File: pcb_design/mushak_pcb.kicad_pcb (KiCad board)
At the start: 2 copper layers, 57.7 x 40 mm, 123 parts, among them J1 Conn_01x04_Male, J10 IR_1, J11 AS5600_1, J12 IR_2, J13 AS5600_2, J14 IR_3, J15 ToF, J16 IR_4, J17 ToF, J2 Conn_01x02_Female, J3 BLE_Conn, J4 AS5600_Left, J5 AS5600_Right, J6 IR_1, J7 IR_3, J8 IR_2, J9 IR_4, M1 motor, M2 motor, Q1 DMN3065LW-7, Q2 DMN3065LW-7, Q3 DMN3065LW-7, Q4 DMN3065LW-7, Q5 DMN3065LW-7, SW1 SW_Push, SW2 SW_Push, U1 BA30BC0FP-E2, U2 AS5048B-HTSP, U3 DRV8833PW, U4 VL6180XV0NR/1, U5 MPU-6500, U6 STM32F405RGTx, U7 AS5048B-HTSP, Y1 25Mhz, Y2 32.769kHz

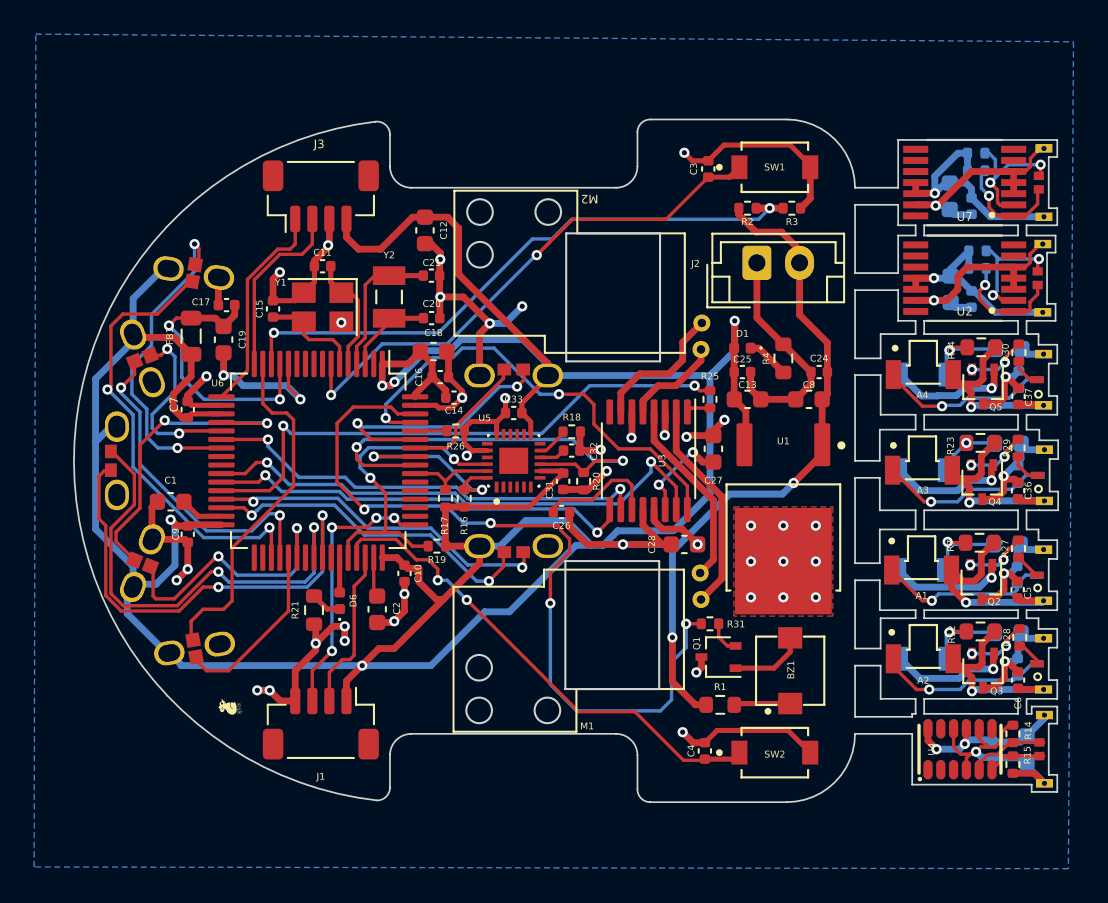
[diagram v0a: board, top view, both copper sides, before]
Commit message: Update PCB as per manufacturing requirements
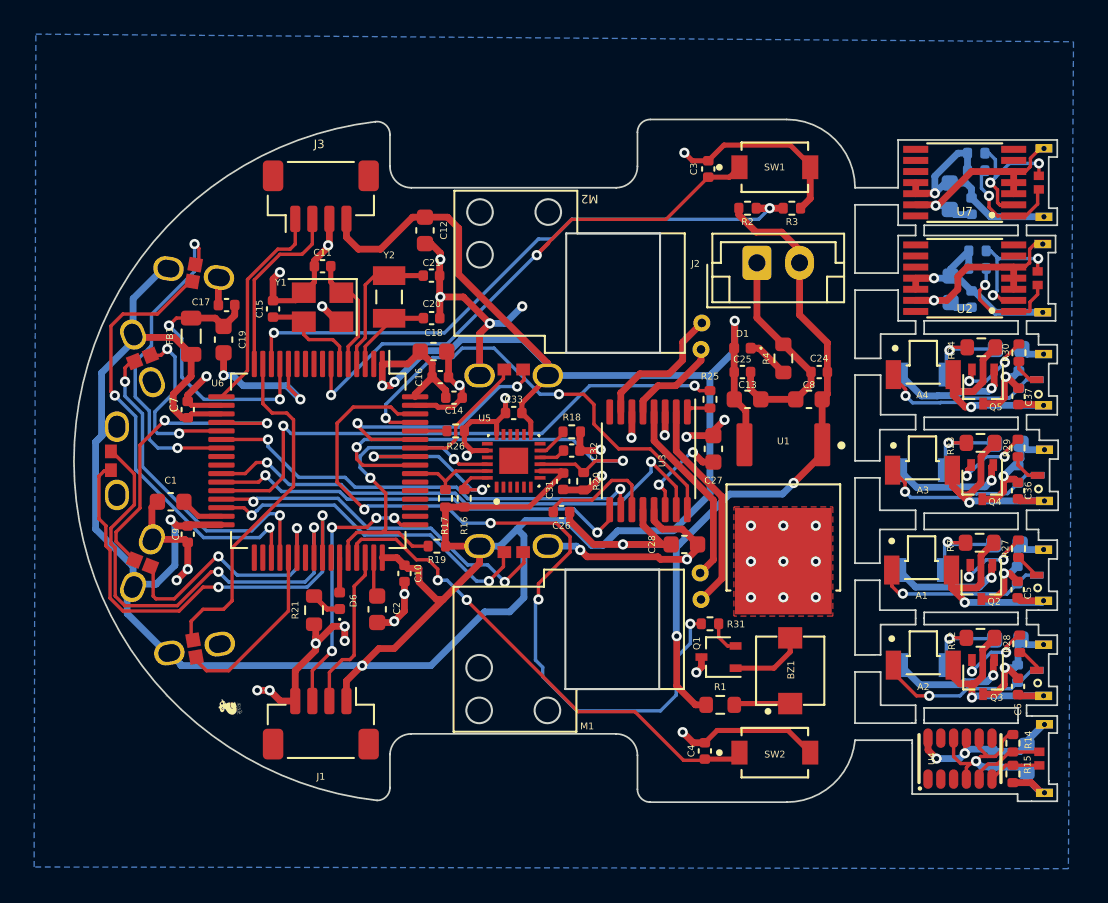
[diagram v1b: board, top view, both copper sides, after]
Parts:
- moved C29 0.55 mm to (204.1, 114.5)
- moved C30 0.55 mm to (202.1, 114.5)
- moved J17 0.55 mm to (205.3, 114.5)
- moved R14 0.55 mm to (203.2, 113.5)
- moved R15 0.55 mm to (203.2, 115.3)
- moved U4 0.55 mm to (200.2, 114.5)
- moved A2 0.37 mm to (198.0, 109.0)
- moved C35 0.37 mm to (202.9, 107.5)
- moved C6 0.37 mm to (203.6, 110.2)
- moved D3 0.37 mm to (198.0, 109.0)
- moved J7 0.37 mm to (205.3, 109.3)
- moved Q3 0.37 mm to (201.5, 109.7)
- moved R11 0.37 mm to (203.5, 109.5)
- moved R12 0.37 mm to (201.3, 107.4)
- moved R28 0.37 mm to (203.7, 107.7)
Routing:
- net POW_GND: track 121.3 -> 132.1 mm, vias 41 -> 42
- net /IR_sensor/+3V0_3: track 12.6 -> 14.4 mm
- net Net-(C38-Pad1): track 3.78 -> 5.44 mm
- net /IR_sensor/+3V0_4: track 12.5 -> 14.0 mm
- net Net-(Q4-Pad2): track 3.51 -> 4.76 mm
- net Net-(Q5-Pad2): track 3.52 -> 4.71 mm
- net Net-(Q2-Pad2): track 3.60 -> 4.69 mm
- net +3V0: track 196.7 -> 195.6 mm
- net Net-(Q3-Pad2): track 3.58 -> 4.54 mm
- net BUZZER_OP: track 46.5 -> 47.1 mm
- net SCL_2: track 20.4 -> 21.0 mm
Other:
- outline, holes or cut-outs redrawn

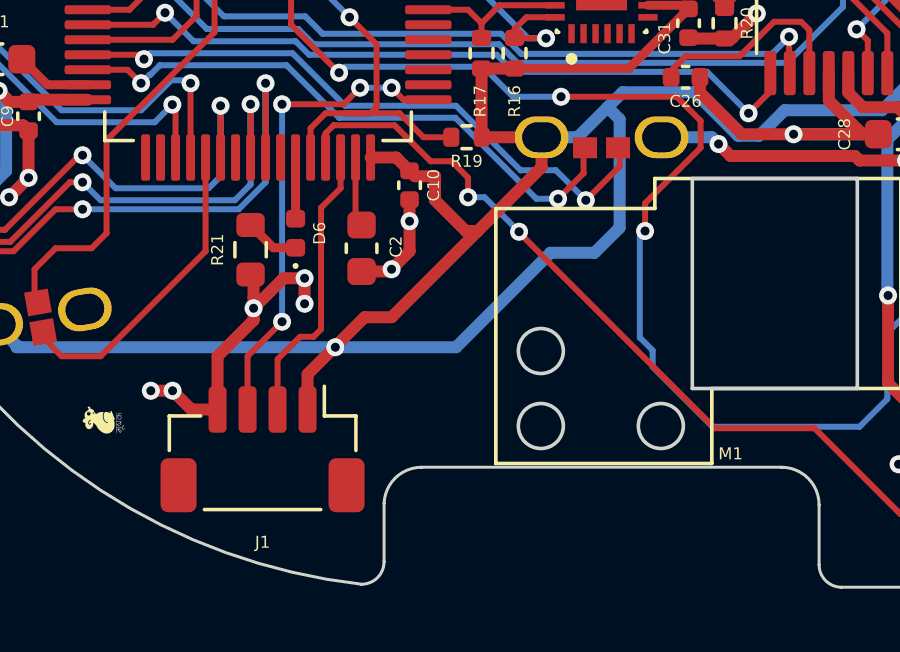
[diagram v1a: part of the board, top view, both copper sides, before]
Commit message: modify silkscreen
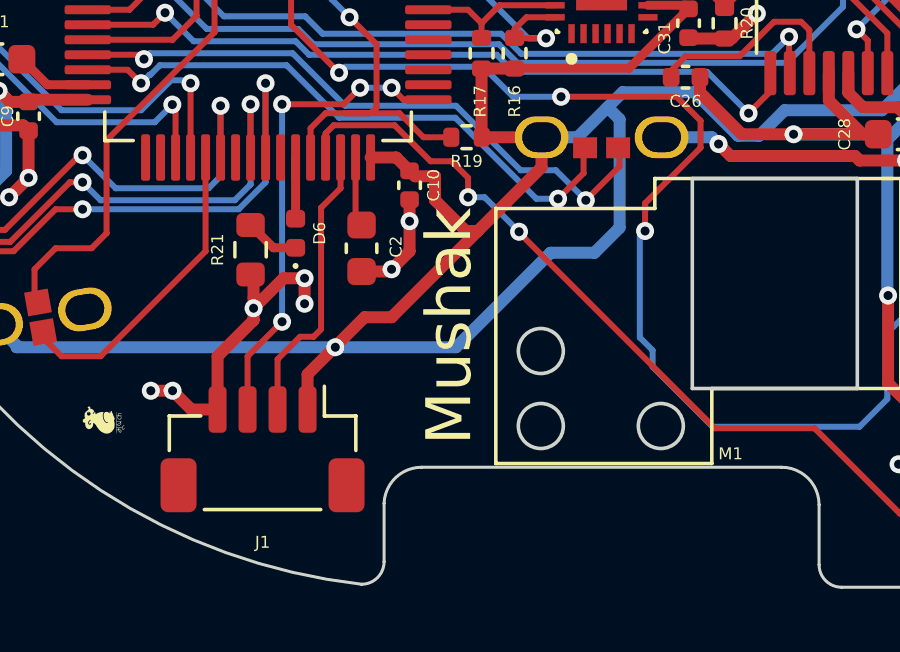
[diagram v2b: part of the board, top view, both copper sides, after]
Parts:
- added REF**: OSHW-Logo2_7.3x6mm_SilkScreen, Symbol:OSHW-Logo2_7.3x6mm_SilkScreen, B.Cu at (173.3, 97.1)
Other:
- board text added: "Mushak"

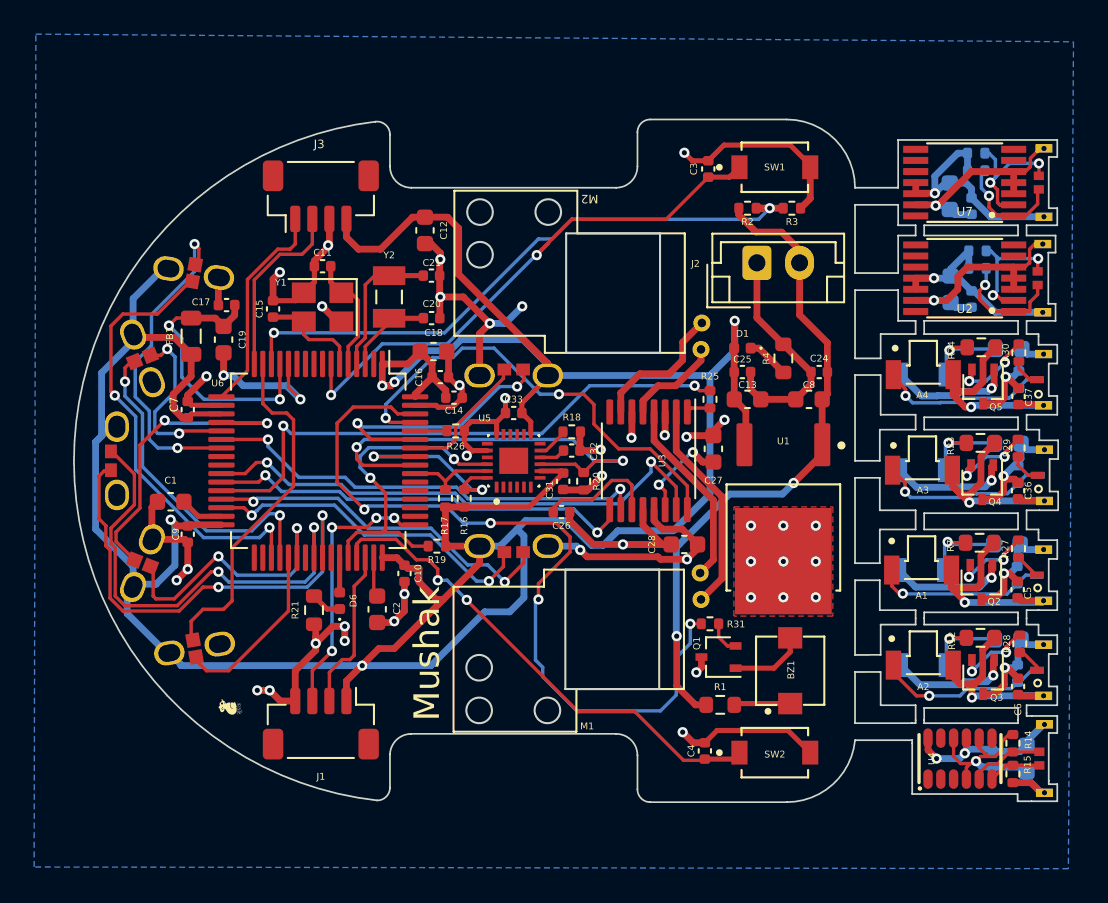
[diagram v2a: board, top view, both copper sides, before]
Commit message: Updated PCB with HTSSOP16 package for DRV8833
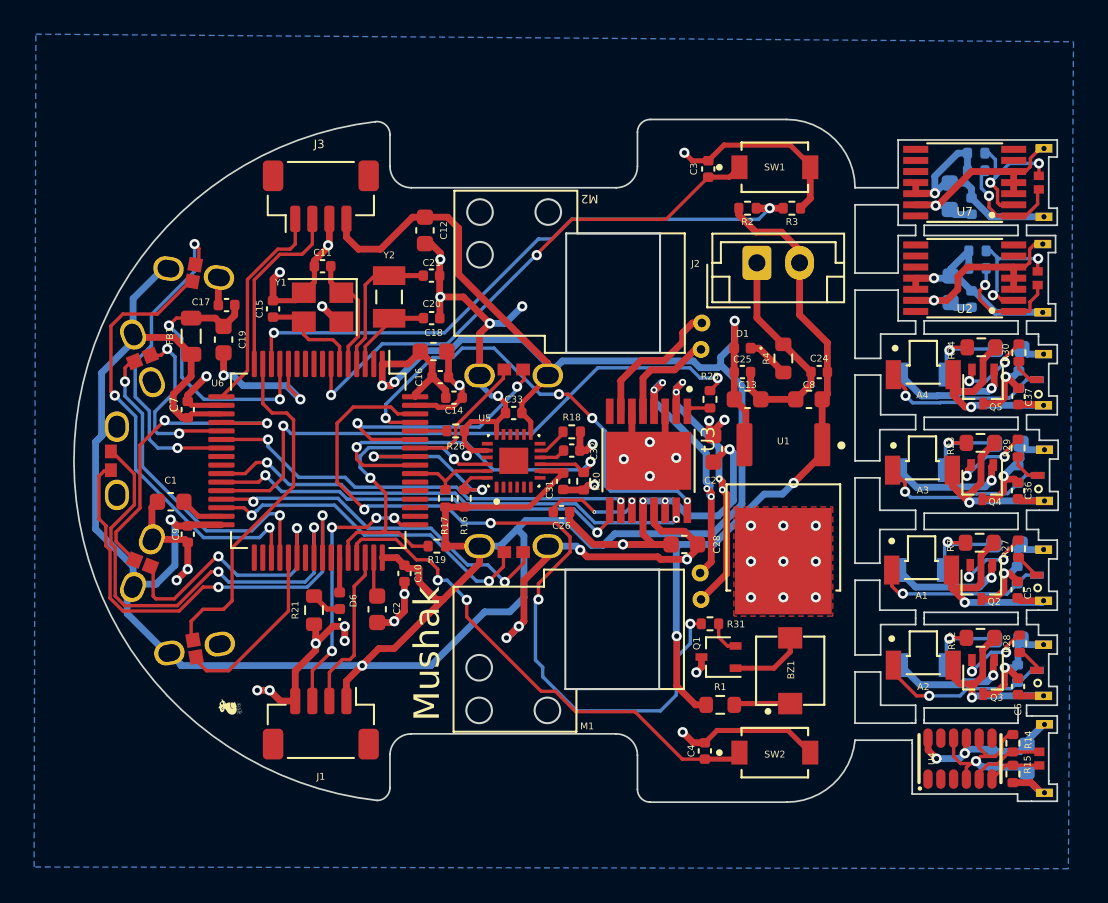
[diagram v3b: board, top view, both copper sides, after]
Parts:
- C20, C21: value 12.5pF -> 12pF
- R25: value 47k -> 4.7k
- U3: value DRV8833PW -> DRV8833PWPR; footprint Package_SO:TSSOP-16_4.4x5mm_P0.65mm -> DRV8833PWPR:IC_DRV8833PWPR
- turned C28 to 180 degrees
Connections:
- C27 pad 2: Net-(C27-Pad2) -> POW_IN
- C28 pad 1: POW_IN -> POW_GND
- C28 pad 2: POW_GND -> POW_IN
- U3 pad 14: Net-(C27-Pad2) -> POW_IN
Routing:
- net POW_IN: track 52.1 -> 63.9 mm, vias 3 -> 6
- net POW_GND: track 132.1 -> 143.2 mm, vias 42 -> 46
- net Net-(M1-Pad2): track 12.6 -> 19.6 mm, vias 0 -> 4
- net Net-(M1-Pad1): track 11.2 -> 17.1 mm, vias 0 -> 4
- net Net-(C27-Pad2): track 5.84 -> 0.00 mm, vias 2 -> 0
- net +3V0: track 195.6 -> 199.1 mm
- net /MPU6500/MISO: track 25.9 -> 22.5 mm
- net /DRV8833_Motor_Driver/AIN2: track 31.2 -> 29.0 mm
- net /DRV8833_Motor_Driver/EN: track 33.4 -> 35.4 mm
- net NRST: track 32.3 -> 31.3 mm
- net /DRV8833_Motor_Driver/BIN2: track 26.5 -> 25.6 mm
- net Net-(C26-Pad2): track 7.05 -> 6.26 mm, vias 0 -> 2
- net /IR_sensor/+3V0_4: track 14.0 -> 13.2 mm
- net /DRV8833_Motor_Driver/AIN1: track 27.1 -> 27.8 mm, vias 2 -> 4
- net DEBUG: track 29.3 -> 29.8 mm
